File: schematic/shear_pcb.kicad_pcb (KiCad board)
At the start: 2 copper layers, 71.1 x 76.2 mm, 11 parts, among them J1 MOTOR1, J2 MOTOR2, J3 LCD_CONN, J4 VIN, J5 ENDSTOP1, J6 ENDSTOP2, U1 Teensy3.5, U2 AMIS30542, U3 AMIS30542

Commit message: Rework circuit board
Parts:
- added C1: 2.2uF, Capacitor_SMD:C_0805_2012Metric_Pad1.15x1.40mm_HandSolder, F.Cu at (124.8, 106.0)
- added C2: 10uF, Capacitor_SMD:C_0805_2012Metric_Pad1.15x1.40mm_HandSolder, F.Cu at (139.7, 116.5)
- added C3: 3.3uF, Capacitor_SMD:C_0805_2012Metric_Pad1.15x1.40mm_HandSolder, F.Cu at (139.7, 111.4)
- added D1: D_Schottky, Diode_SMD:D_0805_2012Metric_Pad1.15x1.40mm_HandSolder, F.Cu at (124.7, 108.6)
- added H1: MountingHole, MountingHole:MountingHole_3.2mm_M3_ISO7380, F.Cu at (192.4, 122.6)
- added H2: MountingHole, MountingHole:MountingHole_3.2mm_M3_ISO7380, F.Cu at (123.2, 122.6)
- added H3: MountingHole, MountingHole:MountingHole_3.2mm_M3_ISO7380, F.Cu at (127.6, 51.4)
- added H4: MountingHole, MountingHole:MountingHole_3.2mm_M3_ISO7380, F.Cu at (192.4, 51.4)
- added L1: 5.6uH, Inductor_SMD:L_Bourns-SRN4018, F.Cu at (135.9, 113.9)
- added U4: R-785.0-1.0, Converter_DCDC:Converter_DCDC_RECOM_R-78E-0.5_THT, F.Cu at (128.9, 112.4)
- R1, R2: footprint Resistor_THT:R_Axial_DIN0204_L3.6mm_D1.6mm_P7.62mm_Horizontal -> Resistor_SMD:R_0805_2012Metric_Pad1.15x1.40mm_HandSolder
- moved R2 40.2 mm to (157.2, 106.7), turned to 180 degrees
- moved U1 32.6 mm to (141.0, 76.8)
- moved J1 32.5 mm to (192.4, 67.9)
- moved J2 32.5 mm to (192.4, 98.4)
- moved U2 32.4 mm to (173.4, 61.6)
- moved U3 32.4 mm to (173.4, 92.1)
- moved J3 31.9 mm to (121.9, 49.5)
- moved J4 31.8 mm to (184.8, 112.4)
- moved J5 31.8 mm to (167.0, 112.4)
- moved J6 31.8 mm to (152.7, 112.4)
- moved R1 25.8 mm to (171.1, 106.7), turned to 180 degrees
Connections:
- J3 pad 1: Net-(J3-Pad1) -> (no net)
- J3 pad 11: Net-(J3-Pad11) -> (no net)
- J3 pad 12: Net-(J3-Pad12) -> (no net)
- J3 pad 18: Net-(J3-Pad18) -> (no net)
- J3 pad 2: Net-(J3-Pad2) -> (no net)
- J3 pad 3: Net-(J3-Pad3) -> (no net)
- J3 pad 4: Net-(J3-Pad4) -> (no net)
- J3 pad 5: Net-(J3-Pad5) -> (no net)
- J3 pad 6: Net-(J3-Pad6) -> (no net)
- U1 pad 10: D\C -> (no net)
- U1 pad 11: CS1 -> D\C
- U1 pad 12: Net-(U1-Pad12) -> CS1
- U1 pad 16: Net-(U1-Pad16) -> (no net)
- U1 pad 17: Net-(U1-Pad17) -> (no net)
- U1 pad 18: Net-(U1-Pad18) -> (no net)
- U1 pad 19: Net-(U1-Pad19) -> (no net)
- U1 pad 2: Net-(U1-Pad2) -> (no net)
- U1 pad 20: Net-(U1-Pad20) -> (no net)
- U1 pad 21: Net-(U1-Pad21) -> (no net)
- U1 pad 22: Net-(U1-Pad22) -> (no net)
- U1 pad 23: YM -> YP
- U1 pad 24: XP -> XM
- U1 pad 25: Net-(U1-Pad25) -> (no net)
- U1 pad 26: Net-(U1-Pad26) -> (no net)
- U1 pad 27: Net-(U1-Pad27) -> (no net)
- U1 pad 28: Net-(U1-Pad28) -> (no net)
- U1 pad 29: Net-(U1-Pad29) -> (no net)
- U1 pad 3: Net-(U1-Pad3) -> (no net)
- U1 pad 32: Net-(U1-Pad32) -> (no net)
- U1 pad 33: Net-(U1-Pad33) -> (no net)
- U1 pad 34: Net-(U1-Pad34) -> (no net)
- U1 pad 35: Net-(U1-Pad35) -> (no net)
- U1 pad 36: Net-(U1-Pad36) -> (no net)
- U1 pad 37: Net-(U1-Pad37) -> (no net)
- U1 pad 38: Net-(U1-Pad38) -> (no net)
- U1 pad 39: Net-(U1-Pad39) -> (no net)
- U1 pad 4: Net-(U1-Pad4) -> (no net)
- U1 pad 41: Net-(U1-Pad41) -> (no net)
- U1 pad 45: Net-(U1-Pad45) -> (no net)
- U1 pad 46: Net-(U1-Pad46) -> (no net)
- U1 pad 47: Net-(U1-Pad47) -> (no net)
- U1 pad 5: Net-(U1-Pad5) -> (no net)
- U1 pad 52: Net-(U1-Pad52) -> (no net)
- U1 pad 53: Net-(U1-Pad53) -> +5V
- U1 pad 54: Net-(U1-Pad54) -> (no net)
- U1 pad 55: Net-(U1-Pad55) -> (no net)
- U1 pad 56: Net-(U1-Pad56) -> (no net)
- U1 pad 57: Net-(U1-Pad57) -> (no net)
- U1 pad 58: Net-(U1-Pad58) -> (no net)
- U1 pad 59: Net-(U1-Pad59) -> (no net)
- U1 pad 6: Net-(U1-Pad6) -> (no net)
- U1 pad 60: Net-(U1-Pad60) -> (no net)
- U1 pad 61: Net-(U1-Pad61) -> (no net)
- U1 pad 62: Net-(U1-Pad62) -> (no net)
- U1 pad 63: Net-(U1-Pad63) -> (no net)
- U1 pad 64: Net-(U1-Pad64) -> (no net)
- U1 pad 65: Net-(U1-Pad65) -> (no net)
- U1 pad 66: Net-(U1-Pad66) -> (no net)
- U1 pad 67: Net-(U1-Pad67) -> (no net)
- U1 pad 68: Net-(U1-Pad68) -> (no net)
- U1 pad 69: Net-(U1-Pad69) -> (no net)
- U1 pad 7: XM -> XP
- U1 pad 70: Net-(U1-Pad70) -> (no net)
- U1 pad 71: Net-(U1-Pad71) -> (no net)
- U1 pad 72: Net-(U1-Pad72) -> (no net)
- U1 pad 73: Net-(U1-Pad73) -> (no net)
- U1 pad 74: Net-(U1-Pad74) -> (no net)
- U1 pad 75: Net-(U1-Pad75) -> (no net)
- U1 pad 76: Net-(U1-Pad76) -> (no net)
- U1 pad 77: Net-(U1-Pad77) -> (no net)
- U1 pad 78: Net-(U1-Pad78) -> (no net)
- U1 pad 79: Net-(U1-Pad79) -> (no net)
- U1 pad 8: Net-(U1-Pad8) -> (no net)
- U1 pad 80: Net-(U1-Pad80) -> (no net)
- U1 pad 81: Net-(U1-Pad81) -> (no net)
- U1 pad 82: Net-(U1-Pad82) -> (no net)
- U1 pad 83: Net-(U1-Pad83) -> (no net)
- U1 pad 84: Net-(U1-Pad84) -> (no net)
- U1 pad 85: Net-(U1-Pad85) -> (no net)
- U1 pad 86: Net-(U1-Pad86) -> (no net)
- U1 pad 9: YP -> YM
- U2 pad 1: Net-(U2-Pad1) -> (no net)
- U2 pad 10: Net-(U2-Pad10) -> (no net)
- U2 pad 11: Net-(U2-Pad11) -> (no net)
- U2 pad 12: Net-(U2-Pad12) -> (no net)
- U2 pad 13: Net-(U2-Pad13) -> (no net)
- U2 pad 3: Net-(U2-Pad3) -> GND
- U3 pad 1: Net-(U3-Pad1) -> (no net)
- U3 pad 10: Net-(U3-Pad10) -> (no net)
- U3 pad 11: Net-(U3-Pad11) -> (no net)
- U3 pad 12: Net-(U3-Pad12) -> (no net)
- U3 pad 13: Net-(U3-Pad13) -> (no net)
- U3 pad 3: Net-(U3-Pad3) -> GND
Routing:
- net +5V: track 0.00 -> 82.6 mm
- net MISO: track 149.1 -> 80.2 mm, vias 4 -> 3
- net MOSI: track 153.2 -> 85.6 mm
- net CLK: track 143.6 -> 87.3 mm, vias 0 -> 1
- net +3V3: track 114.4 -> 167.1 mm, vias 5 -> 1
- net XM: track 8.52 -> 46.0 mm, vias 0 -> 2
- net YM: track 45.7 -> 11.7 mm, vias 2 -> 0
- net XP: track 45.6 -> 14.3 mm, vias 2 -> 1
- net VDC: track 95.2 -> 125.9 mm
- net YP: track 9.57 -> 35.8 mm, vias 0 -> 1
- net GND: track 11.4 -> 0.00 mm, vias 4 -> 0
- net Net-(C3-Pad1): track 0.00 -> 10.8 mm
- net END1: track 24.3 -> 28.8 mm, vias 2 -> 0
- net STEP1: track 9.94 -> 14.4 mm
- net DIR1: track 9.94 -> 14.4 mm
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- added copper zone on F.Cu, net GND
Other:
- board size 71.1 x 76.2 mm -> 78.7 x 81.3 mm
- net class Default: clearance 0.8 -> 0.2; trace_width 0.4 -> 0.3; via_dia 1 -> 0.5; via_drill 0.7 -> 0.25
- net class Motor: clearance 0.8 -> 0.2; via_dia 1 -> 1.2; via_drill 0.7 -> 0.8
- net class Power: clearance 0.8 -> 0.2; via_dia 1 -> 1.2; via_drill 0.7 -> 0.8
- rule trace_clearance: 0.8 -> 0.2
- rule trace_min: 0.4 -> 0.3
- rule via_min_drill: 0.7 -> 0.2
- rule via_min_size: 1 -> 0.5

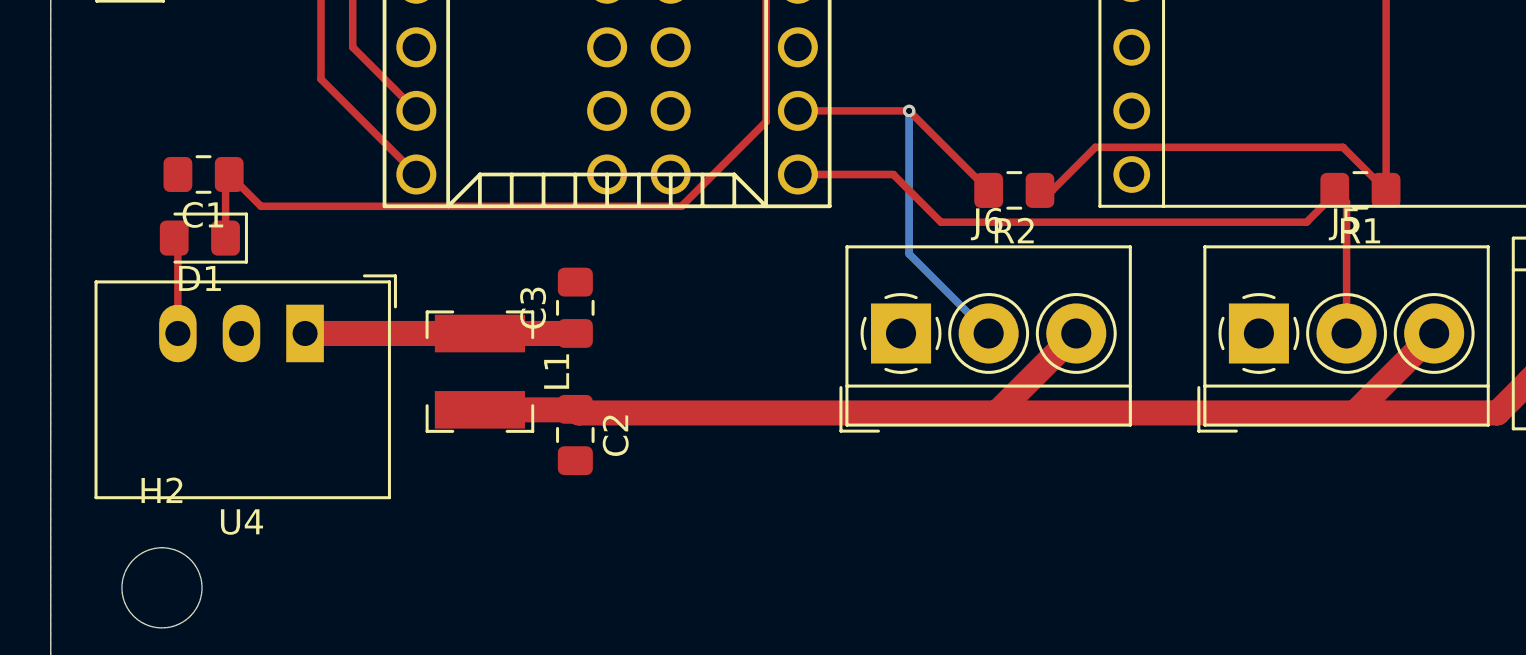
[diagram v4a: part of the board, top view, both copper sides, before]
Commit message: Updated capacitor footprints
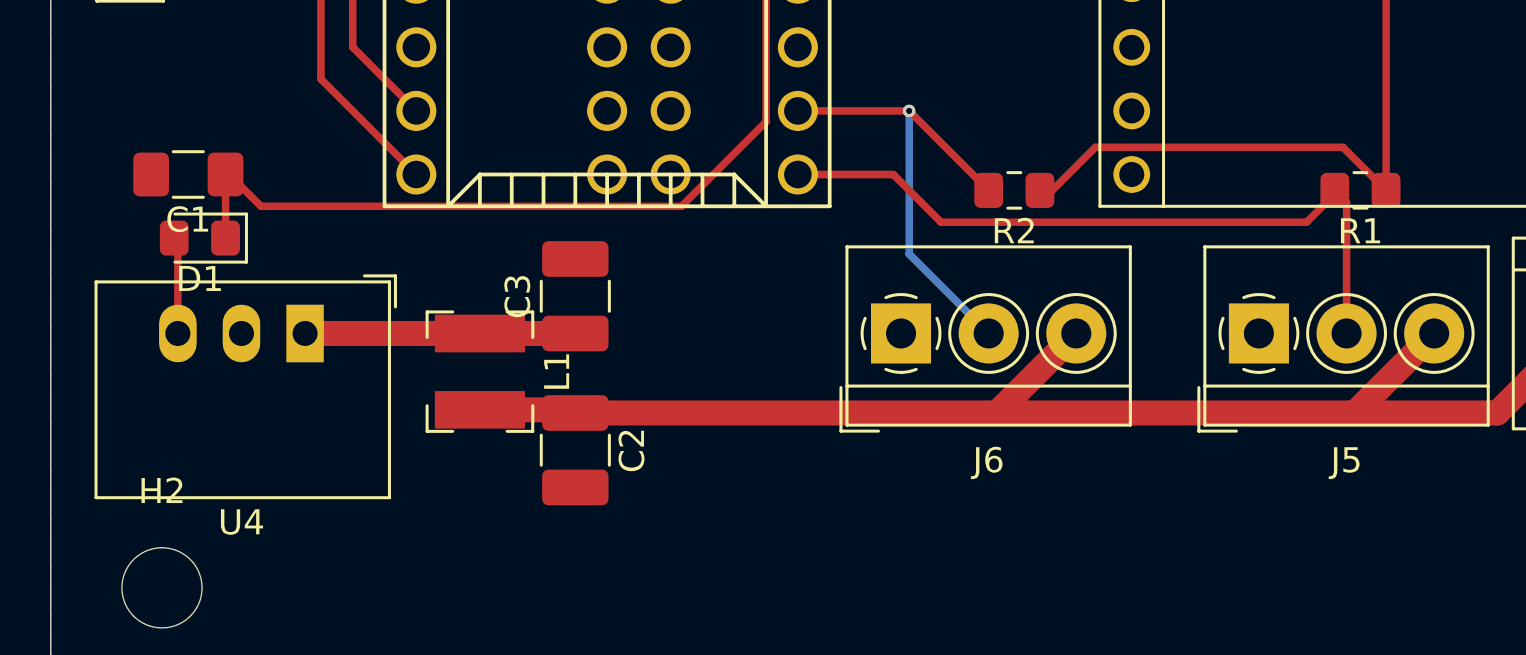
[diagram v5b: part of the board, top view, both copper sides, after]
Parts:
- C1: footprint Capacitor_SMD:C_0805_2012Metric_Pad1.15x1.40mm_HandSolder -> Capacitor_SMD:C_1206_3216Metric_Pad1.42x1.75mm_HandSolder
- C2, C3: footprint Capacitor_SMD:C_0805_2012Metric_Pad1.15x1.40mm_HandSolder -> Capacitor_SMD:C_1210_3225Metric_Pad1.42x2.65mm_HandSolder
- moved C2 0.61 mm to (139.7, 117.1)
- moved C1 0.61 mm to (124.2, 106.0)
- moved C3 0.46 mm to (139.7, 110.9)

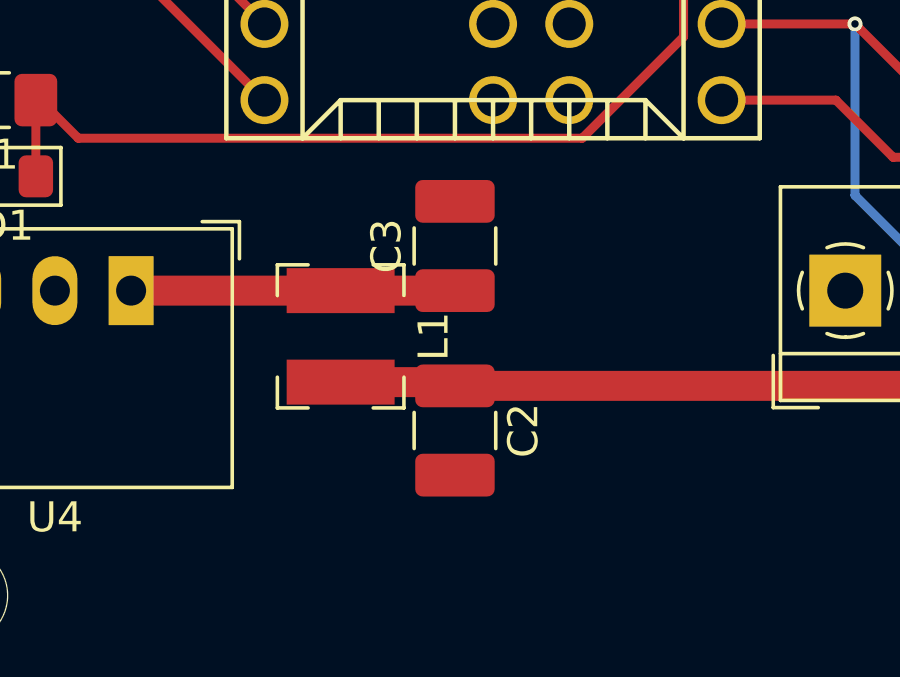
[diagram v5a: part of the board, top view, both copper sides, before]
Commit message: Add CurieOS Logo to board
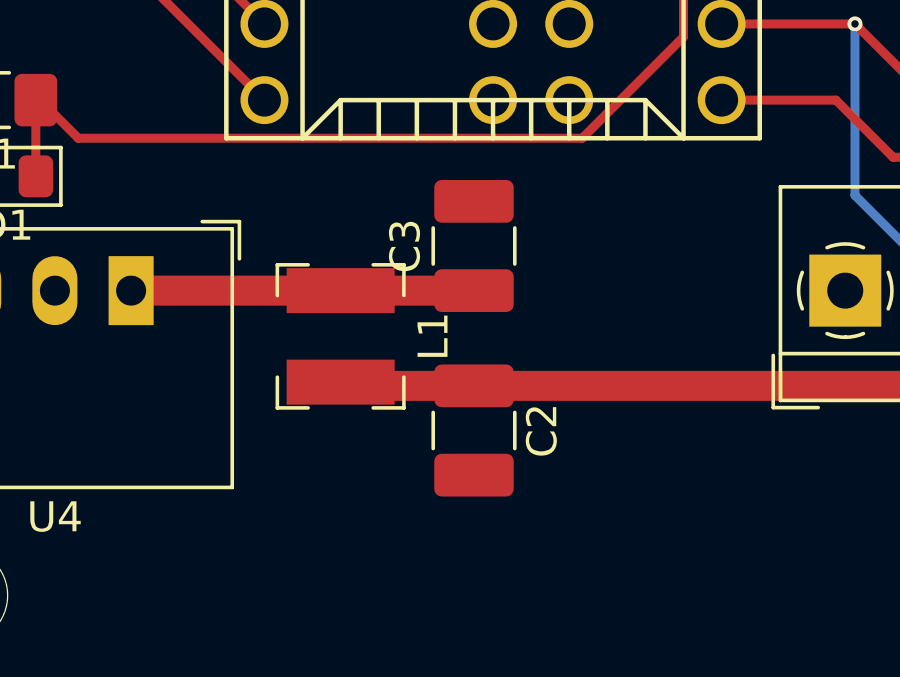
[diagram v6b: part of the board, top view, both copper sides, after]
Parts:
- added G***: LOGO, CurieOS:CurieOS, B.Cu at (172.1, 92.7)
- moved C2 0.64 mm to (140.3, 117.1)
- moved C3 0.64 mm to (140.3, 110.9)
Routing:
- net Net-(C3-Pad1): track 10.8 -> 11.4 mm

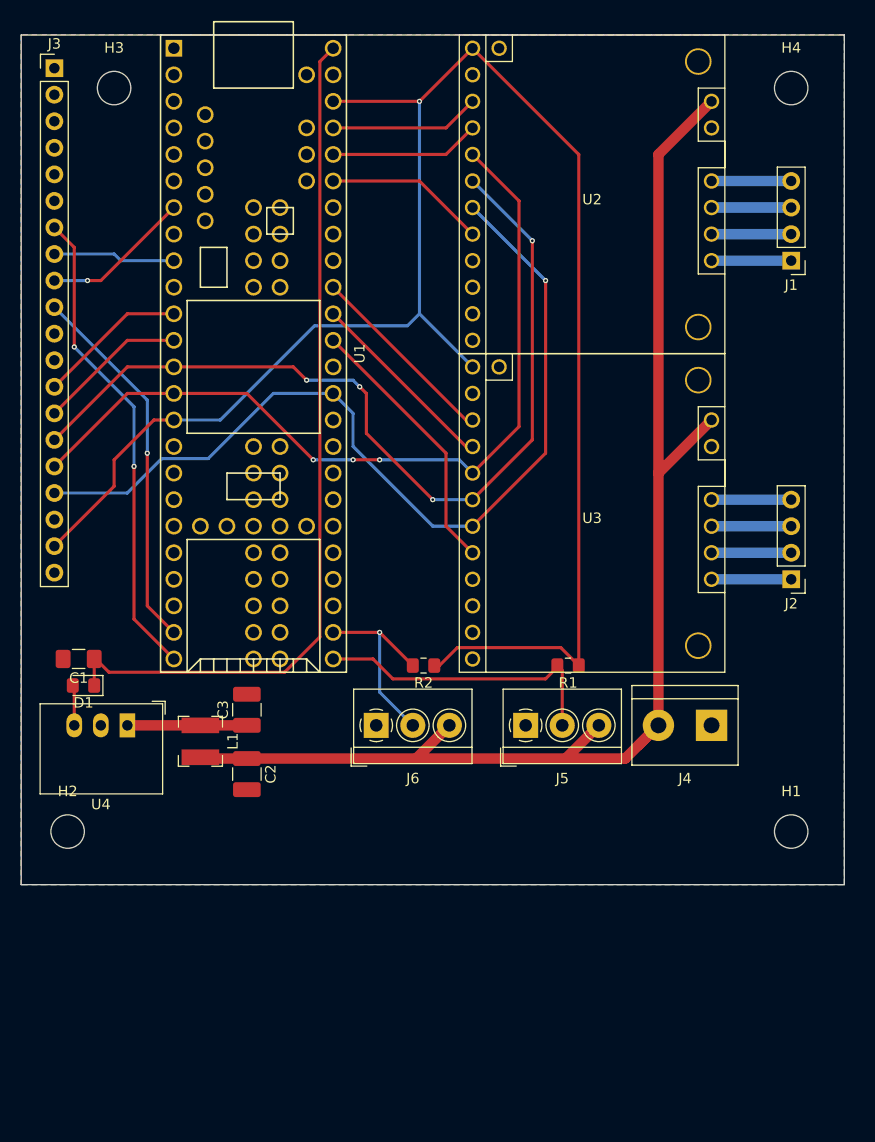
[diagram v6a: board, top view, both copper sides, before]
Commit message: Rebuild board based on feedback
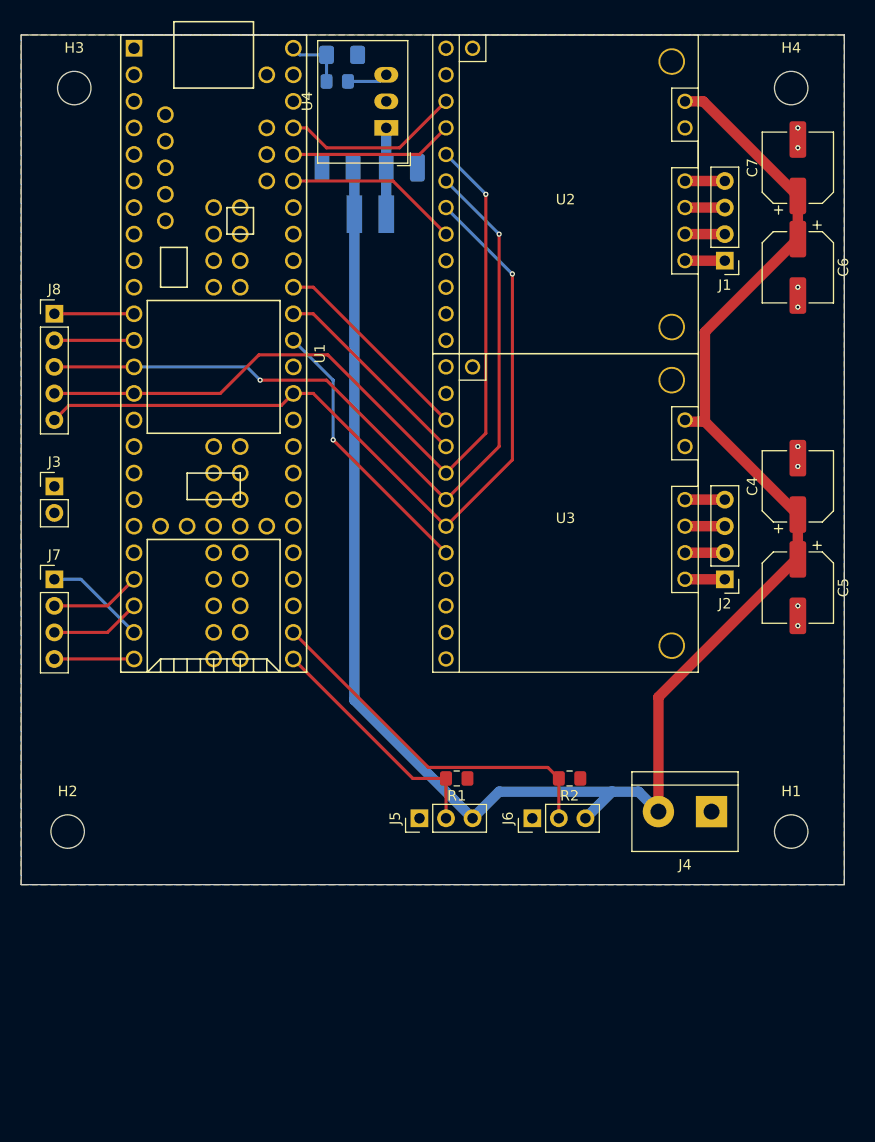
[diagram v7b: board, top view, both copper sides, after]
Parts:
- removed G***: LOGO, CurieOS:CurieOS
- added C4: 10uF, Capacitor_SMD:CP_Elec_6.3x3, F.Cu at (193.0, 89.5)
- added C5: 46uF, Capacitor_SMD:CP_Elec_6.3x3, F.Cu at (193.0, 99.2)
- added C6: 10uF, Capacitor_SMD:CP_Elec_6.3x3, F.Cu at (193.0, 68.6)
- added C7: 47uF, Capacitor_SMD:CP_Elec_6.3x3, F.Cu at (193.0, 59.1)
- added J7: LCD_TOUCH, Connector_PinHeader_2.54mm:PinHeader_1x04_P2.54mm_Vertical, F.Cu at (121.9, 98.4)
- added J8: LCD_SPI, Connector_PinHeader_2.54mm:PinHeader_1x05_P2.54mm_Vertical, F.Cu at (121.9, 73.0)
- C1: value 2.2uF -> 10uF; moved to B.Cu
- C2, C3, D1, L1: moved to B.Cu
- J3: value LCD_CONN -> LCD_POWER; footprint Connector_PinHeader_2.54mm:PinHeader_1x20_P2.54mm_Vertical -> Connector_PinHeader_2.54mm:PinHeader_1x02_P2.54mm_Vertical
- J5, J6: footprint TerminalBlock_4Ucon:TerminalBlock_4Ucon_1x03_P3.50mm_Horizontal -> Connector_PinHeader_2.54mm:PinHeader_1x03_P2.54mm_Vertical
- moved C1 63.0 mm to (149.4, 48.3), turned to 0 degrees
- moved D1 62.7 mm to (149.0, 50.8), turned to 0 degrees
- moved U4 62.3 mm to (153.7, 55.2), turned to 90 degrees
- moved C2 58.6 mm to (149.0, 59.1), turned to 180 degrees
- moved C3 53.9 mm to (155.2, 59.1), turned to 0 degrees
- moved L1 53.0 mm to (152.1, 63.5), turned to 0 degrees
- moved J3 40.0 mm to (121.9, 89.5)
- moved R2 17.7 mm to (171.2, 117.5)
- moved J6 17.4 mm to (167.6, 121.3), turned to 90 degrees
- moved R1 15.2 mm to (160.4, 117.5)
- moved J5 13.5 mm to (156.8, 121.3), turned to 90 degrees
- moved J4 8.26 mm to (184.8, 120.7)
- moved J1 6.35 mm to (186.1, 67.9)
- moved J2 6.35 mm to (186.1, 98.4)
- moved H3 3.81 mm to (123.8, 51.4)
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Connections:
- J3 pad 1: (no net) -> GND
- J3 pad 2: (no net) -> +3V3
- U1 pad 21: (no net) -> XP
- U1 pad 22: (no net) -> YM
- U1 pad 7: XP -> (no net)
- U1 pad 9: YM -> (no net)
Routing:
- net +3V3: track 167.1 -> 0.00 mm, vias 1 -> 0
- net +5V: track 82.6 -> 5.98 mm
- net VDC: track 126.3 -> 178.5 mm
- net XM: track 46.0 -> 7.62 mm, vias 2 -> 0
- net YP: track 35.8 -> 9.72 mm, vias 1 -> 0
- net END2: track 19.1 -> 35.0 mm, vias 1 -> 0
- net MOSI: track 85.6 -> 77.4 mm, vias 4 -> 2
- net CLK: track 87.3 -> 79.5 mm
- net D\C: track 14.3 -> 7.62 mm
- net CS1: track 14.3 -> 7.62 mm
- net END1: track 28.8 -> 23.1 mm
- net XP: track 14.3 -> 8.67 mm, vias 1 -> 0
- net Net-(J2-Pad4): track 7.62 -> 3.81 mm
- net Net-(J2-Pad3): track 7.62 -> 3.81 mm
- net Net-(J2-Pad2): track 7.62 -> 3.81 mm
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- added copper zone on F.Cu, net +3V3
- removed copper zone on F.Cu, net GND
